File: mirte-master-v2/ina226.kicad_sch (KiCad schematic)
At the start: 8 parts, among them U1 INA226

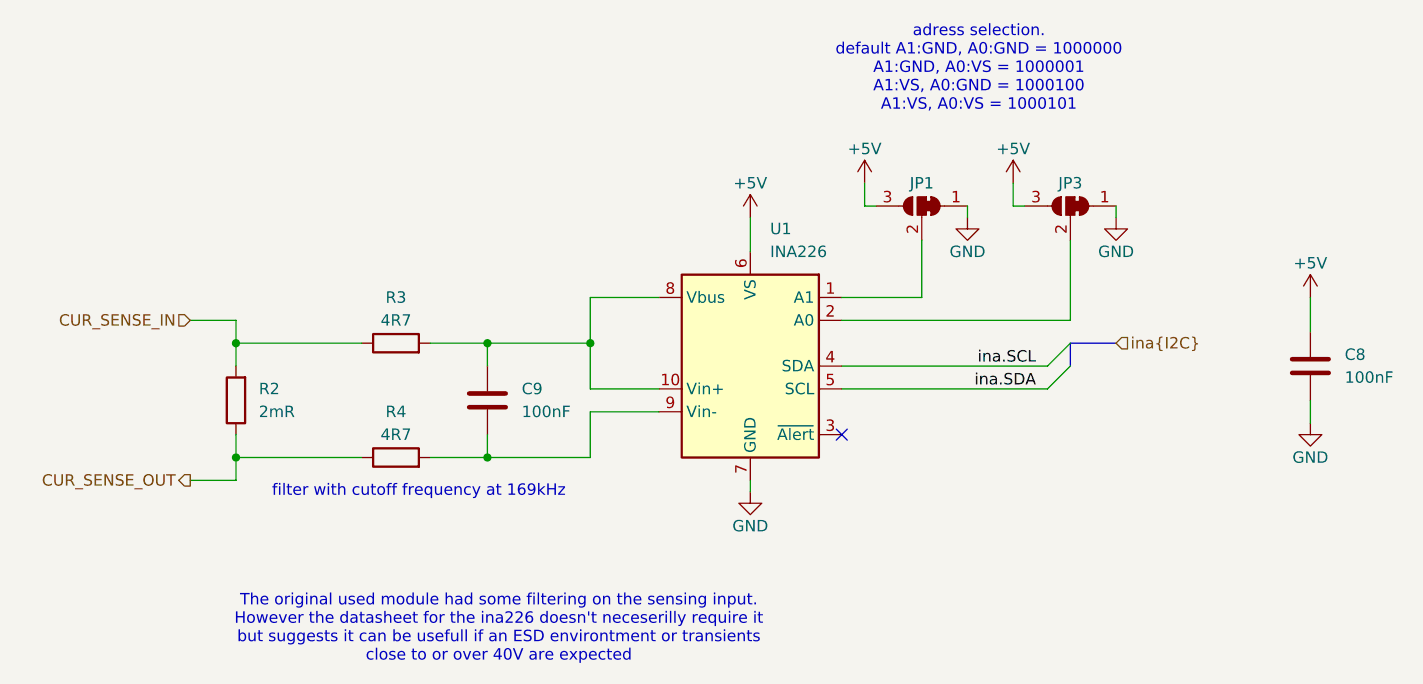
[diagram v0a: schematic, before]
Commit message: integrated the ina226 in the pcb layout
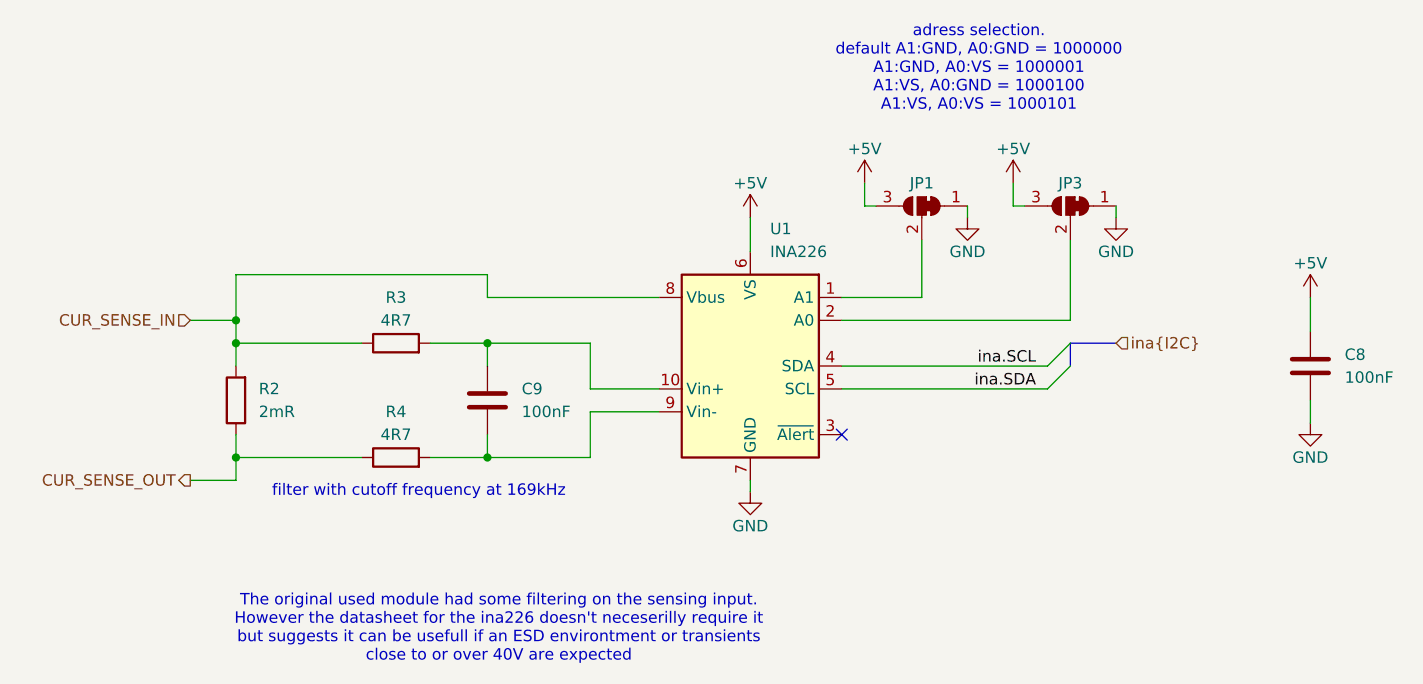
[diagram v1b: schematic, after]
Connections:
- net CUR_SENSE_IN: now also U1.8 (Vbus)
- net at C9.1, R3.2, U1.10 (Vin+): no longer U1.8 (Vbus)
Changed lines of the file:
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@@
-	)
-	(junction
-		(at 133.35 101.6)
-		(diameter 0)
-		(color 0 0 0 0)
 	)
 	(junction
@@
 	)
 	(junction
+		(at 93.98 99.06)
+		(diameter 0)
+		(color 0 0 0 0)
+	)
+	(junction
 		(at 121.92 101.6)
 		(diameter 0)
@@
 	(wire
 		(pts
+			(xy 121.92 93.98) (xy 121.92 96.52)
+		)
+		(stroke
+			(width 0)
+			(type default)
+		)
+	)
+	(wire
+		(pts
 			(xy 121.92 101.6) (xy 121.92 104.14)
 		)
@@
 	(wire
 		(pts
-			(xy 140.97 96.52) (xy 133.35 96.52)
-		)
-		(stroke
-			(width 0)
-			(type default)
-		)
-	)
-	(wire
-		(pts
 			(xy 180.34 83.82) (xy 180.34 86.36)
 		)
@@
 	(wire
 		(pts
+			(xy 93.98 93.98) (xy 93.98 99.06)
+		)
+		(stroke
+			(width 0)
+			(type default)
+		)
+	)
+	(wire
+		(pts
 			(xy 93.98 114.3) (xy 107.95 114.3)
 		)
@@
 	(wire
 		(pts
-			(xy 133.35 96.52) (xy 133.35 101.6)
-		)
-		(stroke
-			(width 0)
-			(type default)
-		)
-	)
-	(wire
-		(pts
 			(xy 133.35 101.6) (xy 133.35 106.68)
 		)
@@
 	(wire
 		(pts
+			(xy 93.98 93.98) (xy 121.92 93.98)
+		)
+		(stroke
+			(width 0)
+			(type default)
+		)
+	)
+	(wire
+		(pts
 			(xy 161.29 106.68) (xy 184.15 106.68)
 		)
 		(stroke
+			(width 0)
+			(type default)
+		)
+	)
+	(wire
+		(pts
+			(xy 121.92 96.52) (xy 140.97 96.52)
+		)
+		(stroke
